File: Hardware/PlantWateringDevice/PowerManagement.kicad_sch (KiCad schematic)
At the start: 14 parts, among them J2 USB_B, M1 Motor_DC, Q1 AO3404A

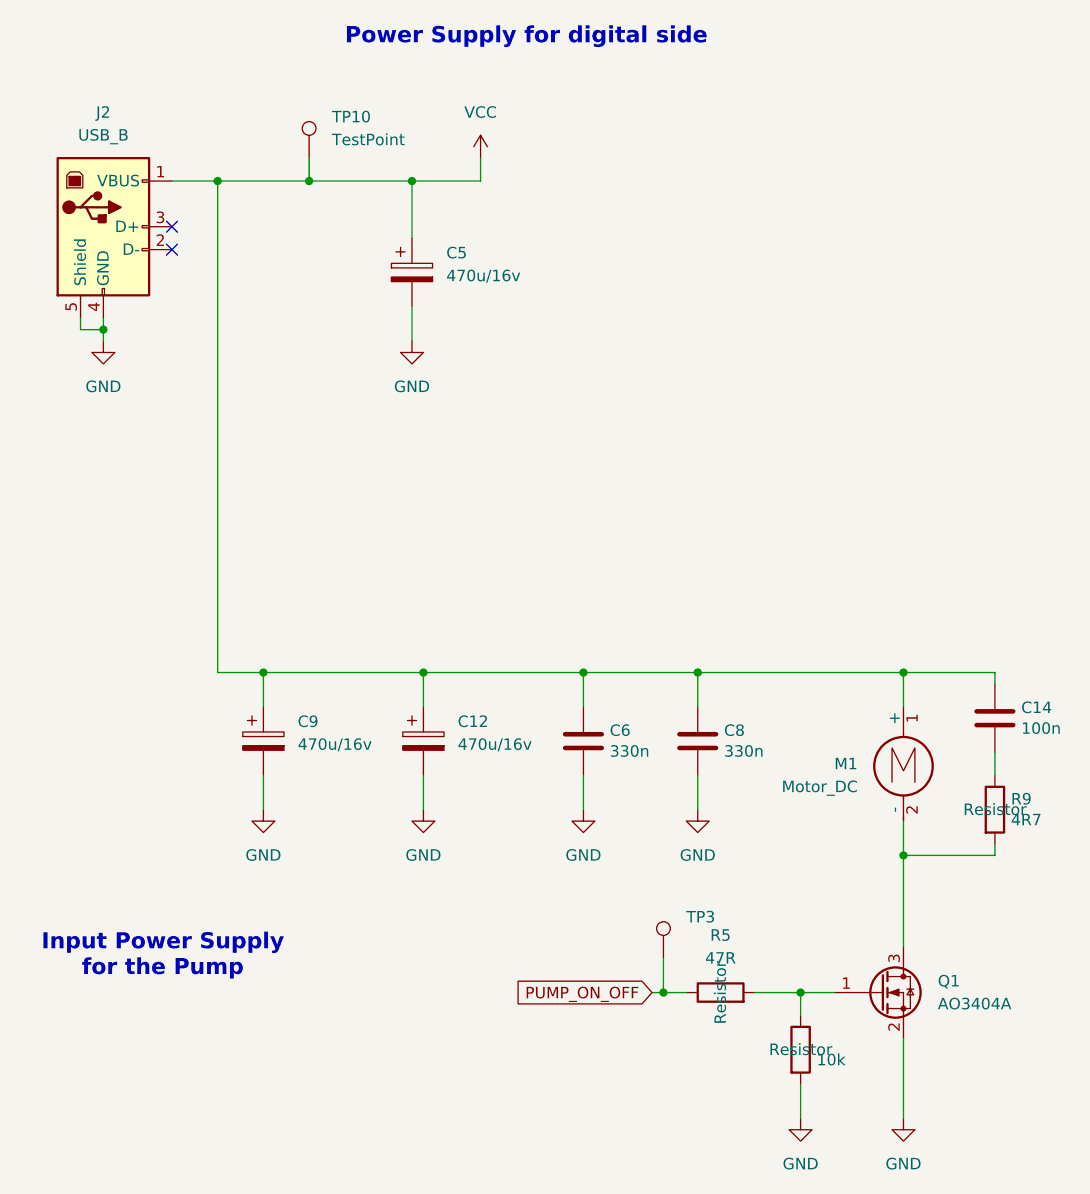
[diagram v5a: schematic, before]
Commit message: fix #16, fix #17, fix #18, fix #19, fix #20, fix #26, fix #27, fix #28, fix #30, fix #32, fix#33, fix #34, fix #35, fix #38
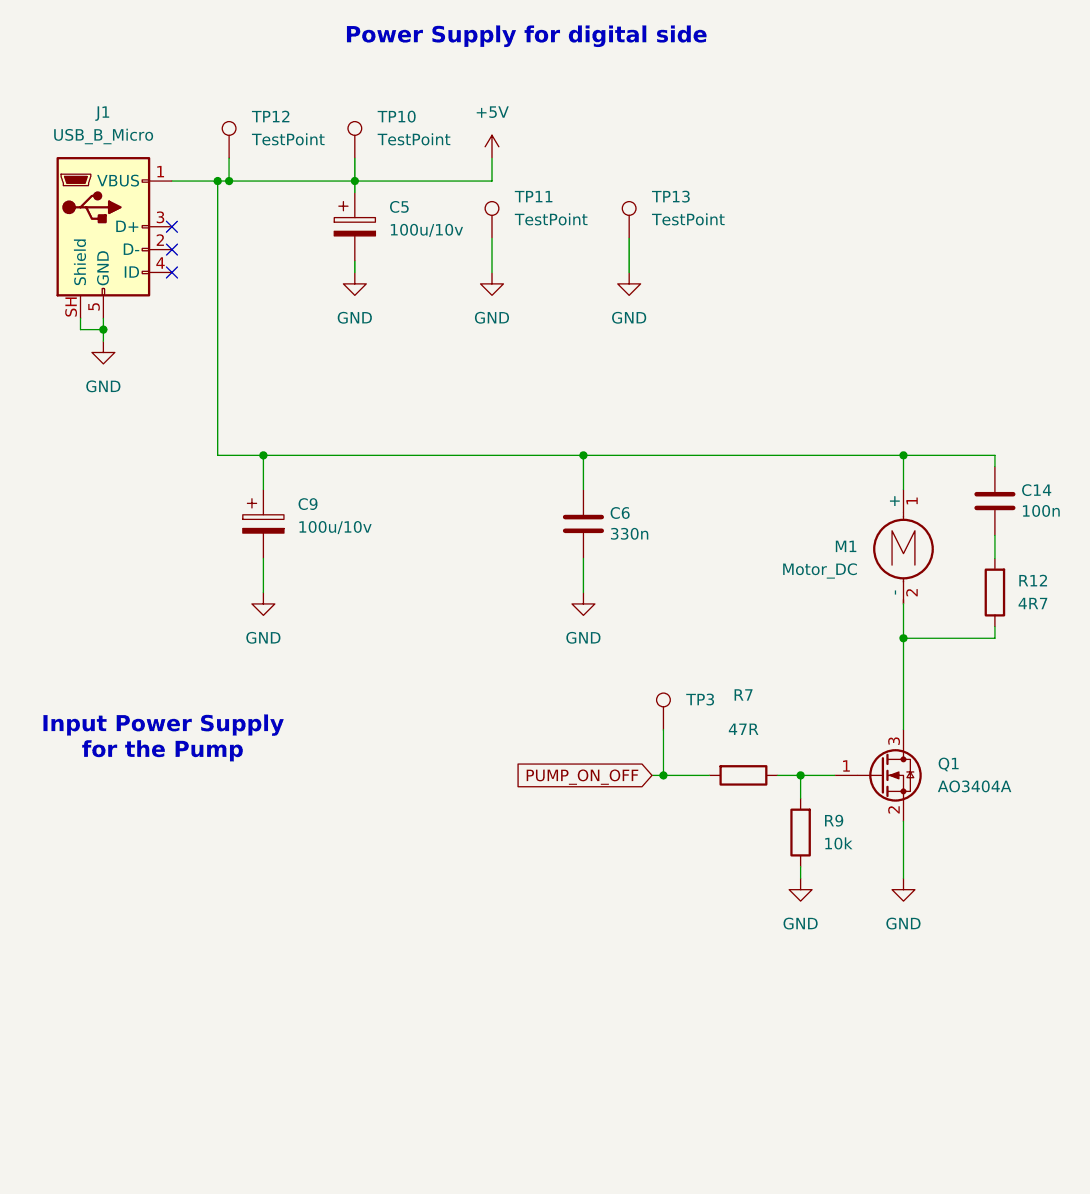
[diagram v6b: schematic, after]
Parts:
- removed C12: 470u/16v, Capacitor_SMD:CP_Elec_8x10, symbol Device:C_Polarized
- removed C8: 330n, Capacitor_SMD:C_0805_2012Metric, symbol Device:C
- removed J2: USB_B, Connector_USB:USB_B_OST_USB-B1HSxx_Horizontal, symbol Connector:USB_B
- removed R5: 47R, Resistor_SMD:R_0805_2012Metric, symbol Device:R
- added J1: USB_B_Micro, PlantWateringDevice:USB_Micro-B_Molex-105017-0001_Extra_Mechanical_Pads, symbol Connector:USB_B_Micro
- added R12: 4R7, Resistor_SMD:R_0603_1608Metric, symbol Device:R
- added TP11, TP12, TP13: TestPoint, TestPoint:TestPoint_Pad_D1.5mm, symbol Connector:TestPoint
- C14, C6: footprint Capacitor_SMD:C_0805_2012Metric -> Capacitor_SMD:C_0603_1608Metric
- C5, C9: value 470u/16v -> 100u/10v; footprint Capacitor_SMD:CP_Elec_8x10 -> Capacitor_Tantalum_SMD:CP_EIA-6032-28_Kemet-C
- M1: footprint Connector_PinHeader_2.54mm:PinHeader_1x02_P2.54mm_Horizontal -> Connector_JST:JST_EH_B2B-EH-A_1x02_P2.50mm_Vertical
- R7: value 10k -> 47R; footprint Resistor_SMD:R_0805_2012Metric -> Resistor_SMD:R_0603_1608Metric
- R9: value 4R7 -> 10k; footprint Resistor_SMD:R_0805_2012Metric -> Resistor_SMD:R_0603_1608Metric
- TP3: footprint TestPoint:TestPoint_Pad_D2.0mm -> TestPoint:TestPoint_Pad_D1.5mm
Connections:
- net GND: now also R9.1, J1.5 (GND), J1.SH (Shield), TP11.1, TP13.1; no longer R7.2
- net PUMP_ON_OFF: now also R7.2
- net at Q1.1 (G), R7.1: now also R9.2
- net at C14.2: now also R12.2; no longer R9.1
- net at M1.2 (-), Q1.3 (D): now also R12.1; no longer R9.2
- net VCC renamed +5V
- net +5V: now also J1.1 (VBUS), TP12.1
- no-connect marks 2 -> 3
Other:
- moved on the sheet: C14, C5, C6, C9, M1, Q1, TP10, TP3

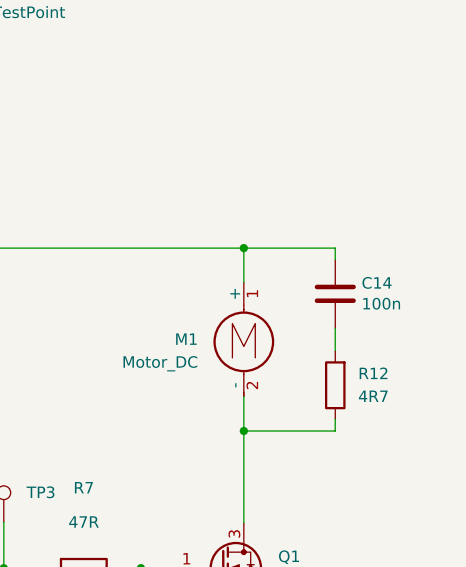
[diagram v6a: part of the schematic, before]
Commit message: firmware implementation in c, draft of unit tests
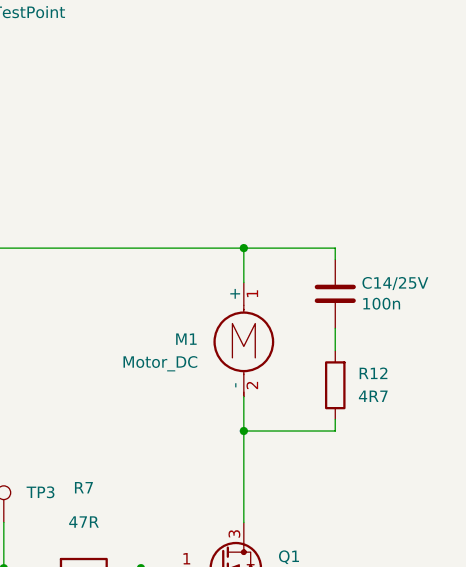
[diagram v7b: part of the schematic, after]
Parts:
- renumbered C14 to C14/25V
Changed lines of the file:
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@@
 		(in_pos_files yes)
 		(dnp no)
-		(property "Reference" "C14"
+		(property "Reference" "C14/25V"
 			(at 171.831 87.7316 0)
 			(show_name no)
@@
 			(project "PlantWateringDevice"
 				(path "/1ef241b3-83d7-48ae-bcca-b7d0eea44e63/0c2157b4-5762-411a-834e-73665a569667"
-					(reference "C14")
+					(reference "C14/25V")
 					(unit 1)
 				)

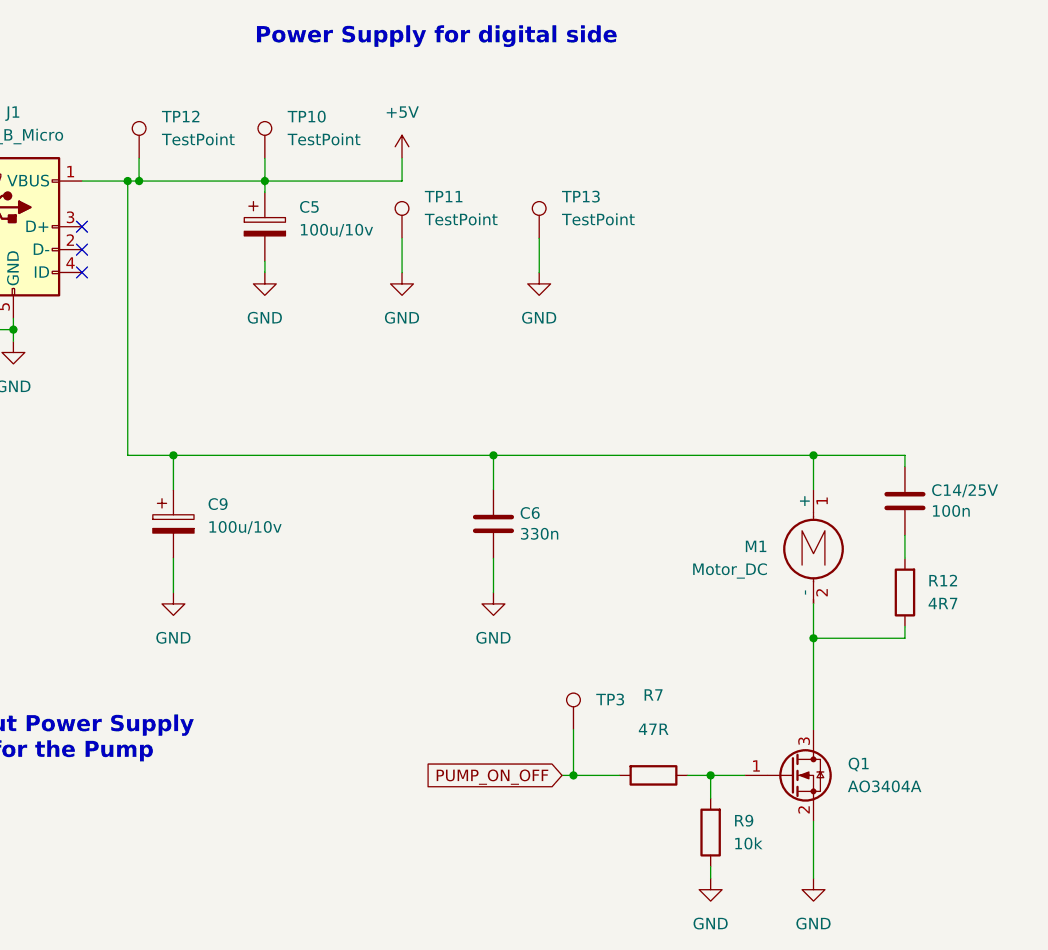
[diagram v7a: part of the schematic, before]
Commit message: hierarchical block diagram structure in kicad
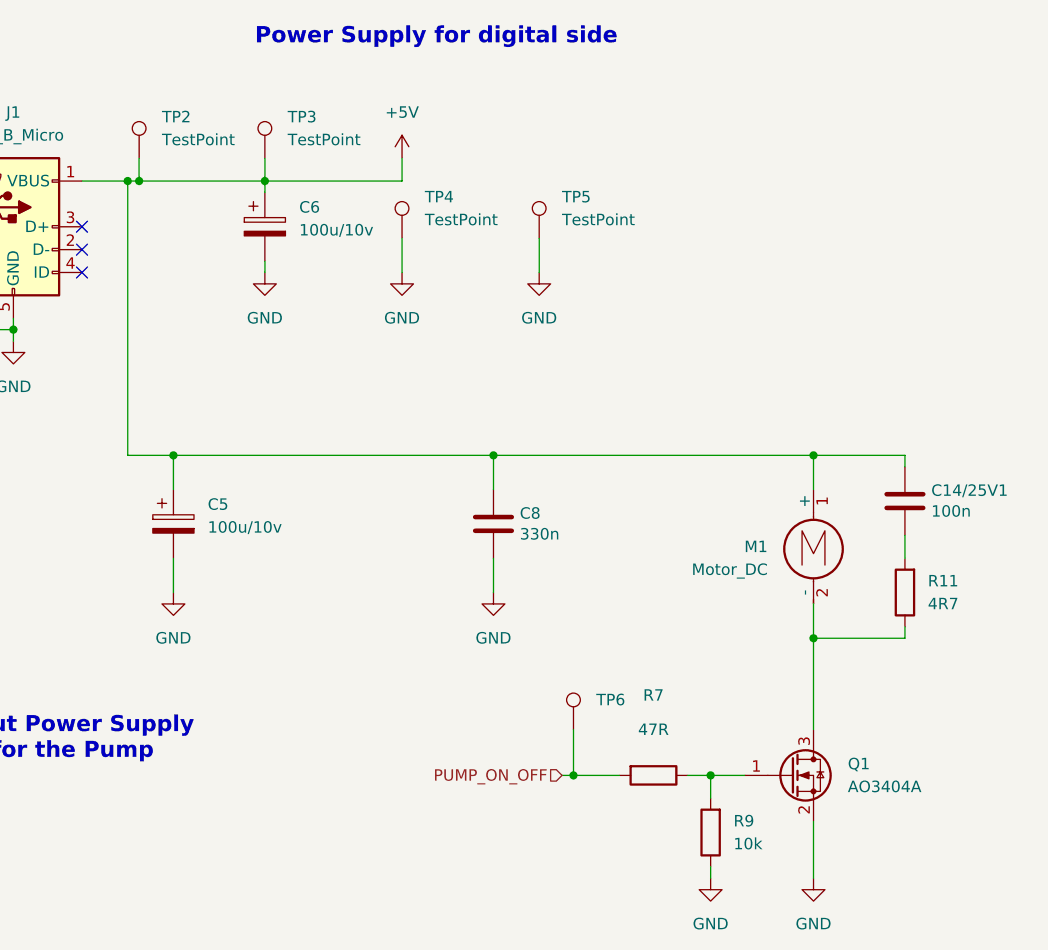
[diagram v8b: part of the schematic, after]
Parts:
- renumbered C14/25V to C14/25V1, C9 to C5, C5 to C6, C6 to C8, R12 to R11, TP12 to TP2, TP10 to TP3, TP11 to TP4, TP13 to TP5, TP3 to TP6
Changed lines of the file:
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@@
 (kicad_sch
-	(version 20260101)
+	(version 20260306)
 	(generator "eeschema")
 	(generator_version "10.0")
@@
 		)
 	)
-	(global_label "PUMP_ON_OFF"
+	(hierarchical_label "PUMP_ON_OFF"
 		(shape input)
 		(at 130.81 119.38 180)
-		(fields_autoplaced yes)
 		(effects
 			(font
@@
 			)
 			(justify right)
-		)
-		(property "Intersheetrefs" "${INTERSHEET_REFS}"
-			(at 114.399 119.38 0)
-			(hide yes)
-			(show_name no)
-			(do_not_autoplace no)
-			(effects
-				(font
-					(size 1.27 1.27)
-				)
-				(justify right)
-			)
 		)
 	)
@@
 		(instances
 			(project "PlantWateringDevice"
-				(path "/1ef241b3-83d7-48ae-bcca-b7d0eea44e63/0c2157b4-5762-411a-834e-73665a569667"
+				(path "/1ef241b3-83d7-48ae-bcca-b7d0eea44e63/a141cb94-983c-4780-96e1-70ed49312478"
 					(reference "#PWR050")
 					(unit 1)
@@
 		(dnp no)
 		(fields_autoplaced yes)
-		(property "Reference" "R12"
+		(property "Reference" "R11"
 			(at 171.45 97.7899 0)
 			(show_name no)
@@
 		(instances
 			(project "PlantWateringDevice"
-				(path "/1ef241b3-83d7-48ae-bcca-b7d0eea44e63/0c2157b4-5762-411a-834e-73665a569667"
-					(reference "R12")
+				(path "/1ef241b3-83d7-48ae-bcca-b7d0eea44e63/a141cb94-983c-4780-96e1-70ed49312478"
+					(reference "R11")
 					(unit 1)
 				)
@@
 		(instances
 			(project "PlantWateringDevice"
-				(path "/1ef241b3-83d7-48ae-bcca-b7d0eea44e63/0c2157b4-5762-411a-834e-73665a569667"
+				(path "/1ef241b3-83d7-48ae-bcca-b7d0eea44e63/a141cb94-983c-4780-96e1-70ed49312478"
 					(reference "#PWR012")
 					(unit 1)
@@
 		(instances
 			(project "PlantWateringDevice"
-				(path "/1ef241b3-83d7-48ae-bcca-b7d0eea44e63/0c2157b4-5762-411a-834e-73665a569667"
+				(path "/1ef241b3-83d7-48ae-bcca-b7d0eea44e63/a141cb94-983c-4780-96e1-70ed49312478"
 					(reference "#PWR028")
 					(unit 1)
@@
 		(dnp no)
 		(fields_autoplaced yes)
-		(property "Reference" "C9"
+		(property "Reference" "C5"
 			(at 91.44 89.2809 0)
 			(show_name no)
@@
 		(instances
 			(project "PlantWateringDevice"
-				(path "/1ef241b3-83d7-48ae-bcca-b7d0eea44e63/0c2157b4-5762-411a-834e-73665a569667"
-					(reference "C9")
+				(path "/1ef241b3-83d7-48ae-bcca-b7d0eea44e63/a141cb94-983c-4780-96e1-70ed49312478"
+					(reference "C5")
 					(unit 1)
 				)
@@
 		(dnp no)
 		(fields_autoplaced yes)
-		(property "Reference" "TP13"
+		(property "Reference" "TP5"
 			(at 130.81 55.1179 0)
 			(show_name no)
@@
 		(instances
 			(project "PlantWateringDevice"
-				(path "/1ef241b3-83d7-48ae-bcca-b7d0eea44e63/0c2157b4-5762-411a-834e-73665a569667"
-					(reference "TP13")
+				(path "/1ef241b3-83d7-48ae-bcca-b7d0eea44e63/a141cb94-983c-4780-96e1-70ed49312478"
+					(reference "TP5")
 					(unit 1)
 				)
@@
 		(instances
 			(project "PlantWateringDevice"
-				(path "/1ef241b3-83d7-48ae-bcca-b7d0eea44e63/0c2157b4-5762-411a-834e-73665a569667"
+				(path "/1ef241b3-83d7-48ae-bcca-b7d0eea44e63/a141cb94-983c-4780-96e1-70ed49312478"
 					(reference "#PWR051")
 					(unit 1)
@@
 		(dnp no)
 		(fields_autoplaced yes)
-		(property "Reference" "C5"
+		(property "Reference" "C6"
 			(at 101.6 56.2609 0)
 			(show_name no)
@@
 		(instances
 			(project "PlantWateringDevice"
-				(path "/1ef241b3-83d7-48ae-bcca-b7d0eea44e63/0c2157b4-5762-411a-834e-73665a569667"
-					(reference "C5")
+				(path "/1ef241b3-83d7-48ae-bcca-b7d0eea44e63/a141cb94-983c-4780-96e1-70ed49312478"
+					(reference "C6")
 					(unit 1)
 				)
@@
 		(instances
 			(project "PlantWateringDevice"
-				(path "/1ef241b3-83d7-48ae-bcca-b7d0eea44e63/0c2157b4-5762-411a-834e-73665a569667"
+				(path "/1ef241b3-83d7-48ae-bcca-b7d0eea44e63/a141cb94-983c-4780-96e1-70ed49312478"
 					(reference "R9")
 					(unit 1)
@@
 		)
 		(instances
-			(project ""
-				(path "/1ef241b3-83d7-48ae-bcca-b7d0eea44e63/0c2157b4-5762-411a-834e-73665a569667"
+			(project "PlantWateringDevice"
+				(path "/1ef241b3-83d7-48ae-bcca-b7d0eea44e63/a141cb94-983c-4780-96e1-70ed49312478"
 					(reference "M1")
 					(unit 1)
@@
 		(dnp no)
 		(fields_autoplaced yes)
-		(property "Reference" "TP3"
+		(property "Reference" "TP6"
 			(at 134.62 110.9979 0)
 			(show_name no)
@@
 		(instances
 			(project "PlantWateringDevice"
-				(path "/1ef241b3-83d7-48ae-bcca-b7d0eea44e63/0c2157b4-5762-411a-834e-73665a569667"
-					(reference "TP3")
+				(path "/1ef241b3-83d7-48ae-bcca-b7d0eea44e63/a141cb94-983c-4780-96e1-70ed49312478"
+					(reference "TP6")
 					(unit 1)
 				)
@@
 		(instances
 			(project "PlantWateringDevice"
-				(path "/1ef241b3-83d7-48ae-bcca-b7d0eea44e63/0c2157b4-5762-411a-834e-73665a569667"
+				(path "/1ef241b3-83d7-48ae-bcca-b7d0eea44e63/a141cb94-983c-4780-96e1-70ed49312478"
 					(reference "#PWR06")
 					(unit 1)
@@
 		(instances
 			(project "PlantWateringDevice"
-				(path "/1ef241b3-83d7-48ae-bcca-b7d0eea44e63/0c2157b4-5762-411a-834e-73665a569667"
+				(path "/1ef241b3-83d7-48ae-bcca-b7d0eea44e63/a141cb94-983c-4780-96e1-70ed49312478"
 					(reference "#PWR026")
 					(unit 1)
@@
 		(dnp no)
 		(fields_autoplaced yes)
-		(property "Reference" "TP12"
+		(property "Reference" "TP2"
 			(at 86.36 46.2279 0)
 			(show_name no)
@@
 		(instances
 			(project "PlantWateringDevice"
-				(path "/1ef241b3-83d7-48ae-bcca-b7d0eea44e63/0c2157b4-5762-411a-834e-73665a569667"
-					(reference "TP12")
+				(path "/1ef241b3-83d7-48ae-bcca-b7d0eea44e63/a141cb94-983c-4780-96e1-70ed49312478"
+					(reference "TP2")
 					(unit 1)
 				)
@@
 		(dnp no)
 		(fields_autoplaced yes)
-		(property "Reference" "TP10"
+		(property "Reference" "TP3"
 			(at 100.33 46.2279 0)
 			(show_name no)
@@
 		(instances
 			(project "PlantWateringDevice"
-				(path "/1ef241b3-83d7-48ae-bcca-b7d0eea44e63/0c2157b4-5762-411a-834e-73665a569667"
-					(reference "TP10")
+				(path "/1ef241b3-83d7-48ae-bcca-b7d0eea44e63/a141cb94-983c-4780-96e1-70ed49312478"
+					(reference "TP3")
 					(unit 1)
 				)
@@
 		(instances
 			(project "PlantWateringDevice"
-				(path "/1ef241b3-83d7-48ae-bcca-b7d0eea44e63/0c2157b4-5762-411a-834e-73665a569667"
+				(path "/1ef241b3-83d7-48ae-bcca-b7d0eea44e63/a141cb94-983c-4780-96e1-70ed49312478"
 					(reference "#PWR011")
 					(unit 1)
@@
 		(instances
 			(project "PlantWateringDevice"
-				(path "/1ef241b3-83d7-48ae-bcca-b7d0eea44e63/0c2157b4-5762-411a-834e-73665a569667"
+				(path "/1ef241b3-83d7-48ae-bcca-b7d0eea44e63/a141cb94-983c-4780-96e1-70ed49312478"
 					(reference "#PWR052")
 					(unit 1)
@@
 		(in_pos_files yes)
 		(dnp no)
-		(property "Reference" "C14/25V"
+		(property "Reference" "C14/25V1"
 			(at 171.831 87.7316 0)
 			(show_name no)
@@
 		(instances
 			(project "PlantWateringDevice"
-				(path "/1ef241b3-83d7-48ae-bcca-b7d0eea44e63/0c2157b4-5762-411a-834e-73665a569667"
-					(reference "C14/25V")
+				(path "/1ef241b3-83d7-48ae-bcca-b7d0eea44e63/a141cb94-983c-4780-96e1-70ed49312478"
+					(reference "C14/25V1")
 					(unit 1)
 				)
@@
 		(instances
 			(project "PlantWateringDevice"
-				(path "/1ef241b3-83d7-48ae-bcca-b7d0eea44e63/0c2157b4-5762-411a-834e-73665a569667"
+				(path "/1ef241b3-83d7-48ae-bcca-b7d0eea44e63/a141cb94-983c-4780-96e1-70ed49312478"
 					(reference "R7")
 					(unit 1)
@@
 		(instances
 			(project "PlantWateringDevice"
-				(path "/1ef241b3-83d7-48ae-bcca-b7d0eea44e63/0c2157b4-5762-411a-834e-73665a569667"
+				(path "/1ef241b3-83d7-48ae-bcca-b7d0eea44e63/a141cb94-983c-4780-96e1-70ed49312478"
 					(reference "#PWR018")
 					(unit 1)
@@
 		)
 		(instances
-			(project ""
-				(path "/1ef241b3-83d7-48ae-bcca-b7d0eea44e63/0c2157b4-5762-411a-834e-73665a569667"
+			(project "PlantWateringDevice"
+				(path "/1ef241b3-83d7-48ae-bcca-b7d0eea44e63/a141cb94-983c-4780-96e1-70ed49312478"
 					(reference "J1")
 					(unit 1)
@@
 		)
 		(instances
-			(project ""
-				(path "/1ef241b3-83d7-48ae-bcca-b7d0eea44e63/0c2157b4-5762-411a-834e-73665a569667"
+			(project "PlantWateringDevice"
+				(path "/1ef241b3-83d7-48ae-bcca-b7d0eea44e63/a141cb94-983c-4780-96e1-70ed49312478"
 					(reference "Q1")
 					(unit 1)
@@
 		(in_pos_files yes)
 		(dnp no)
-		(property "Reference" "C6"
+		(property "Reference" "C8"
 			(at 126.111 90.2716 0)
 			(show_name no)
@@
 		(instances
 			(project "PlantWateringDevice"
-				(path "/1ef241b3-83d7-48ae-bcca-b7d0eea44e63/0c2157b4-5762-411a-834e-73665a569667"
-					(reference "C6")
+				(path "/1ef241b3-83d7-48ae-bcca-b7d0eea44e63/a141cb94-983c-4780-96e1-70ed49312478"
+					(reference "C8")
 					(unit 1)
 				)
@@
 		(dnp no)
 		(fields_autoplaced yes)
-		(property "Reference" "TP11"
+		(property "Reference" "TP4"
 			(at 115.57 55.1179 0)
 			(show_name no)
@@
 		(instances
 			(project "PlantWateringDevice"
-				(path "/1ef241b3-83d7-48ae-bcca-b7d0eea44e63/0c2157b4-5762-411a-834e-73665a569667"
-					(reference "TP11")
+				(path "/1ef241b3-83d7-48ae-bcca-b7d0eea44e63/a141cb94-983c-4780-96e1-70ed49312478"
+					(reference "TP4")
 					(unit 1)
 				)
